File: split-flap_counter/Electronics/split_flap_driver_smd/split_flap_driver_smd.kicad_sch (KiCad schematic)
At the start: 34 parts, among them J1 MOT1, J2 MOT1, J3 endSW1, J4 PWR, J5 endSW2, J6 button1, J7 button2, Q1 MMBT3904, U1 ULN2003A, U3 ATtiny2313-20M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

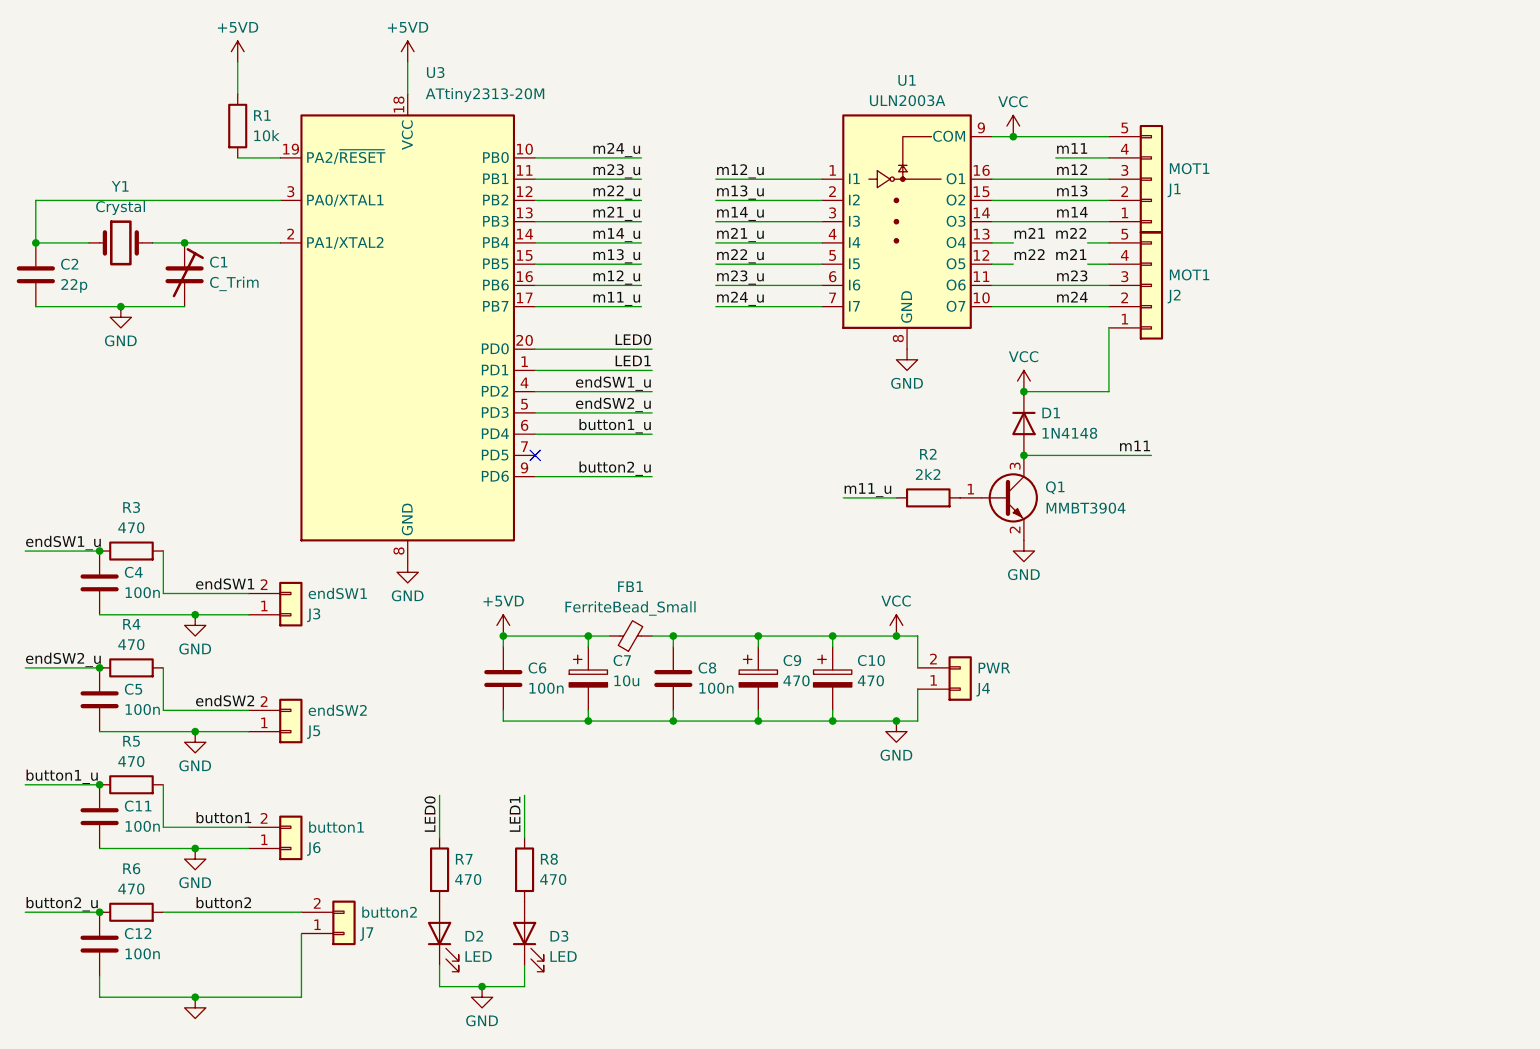
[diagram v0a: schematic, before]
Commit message: added SMD PCB version
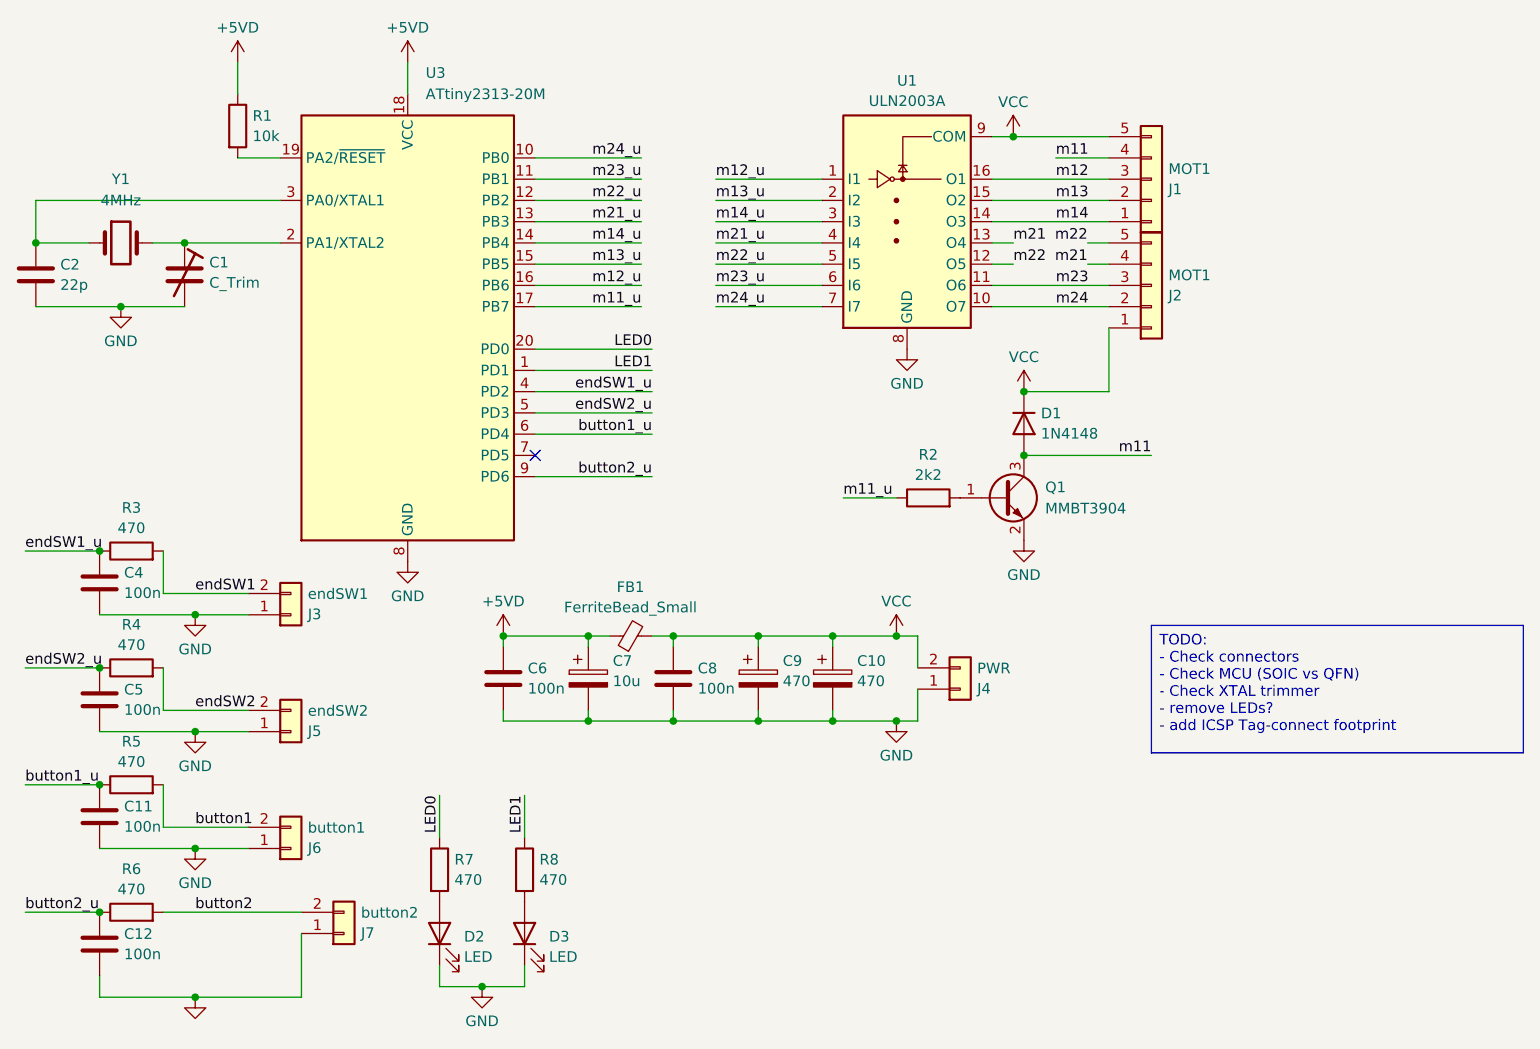
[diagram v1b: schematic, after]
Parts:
- Y1: value Crystal -> 4MHz
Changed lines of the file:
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@@
 		(company "Xavier Bourlot")
 	)
+	(text_box "TODO:\n- Check connectors\n- Check MCU (SOIC vs QFN)\n- Check XTAL trimmer\n- remove LEDs?\n- add ICSP Tag-connect footprint"
+		(exclude_from_sim no)
+		(at 149.86 86.36 0)
+		(size 44.45 15.24)
+		(margins 0.9525 0.9525 0.9525 0.9525)
+		(stroke
+			(width 0)
+			(type solid)
+		)
+		(fill
+			(type color)
+			(color 255 255 194 1)
+		)
+		(effects
+			(font
+				(size 1.27 1.27)
+			)
+			(justify left top)
+		)
+	)
 	(junction
 		(at 134.62 66.04)
@@
 		(fields_autoplaced yes)
 		(property "Reference" "Y1"
-			(at 26.67 33.9301 0)
+			(at 26.67 33.02 0)
 			(effects
 				(font
@@
 			)
 		)
-		(property "Value" "Crystal"
-			(at 26.67 36.3544 0)
+		(property "Value" "4MHz"
+			(at 26.67 35.56 0)
 			(effects
 				(font
